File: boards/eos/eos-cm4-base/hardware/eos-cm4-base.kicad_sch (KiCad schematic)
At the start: 43 parts, among them J1 CM4 1-100, J2 CM4 101-200, J3 USB-C, J4 USB-A, J5 TRJG0926HENL, J6 microSD, J7 GPIO, J8 FAN, J9 BOOT, Q1 BSS84, SW1 RESET, U1 USBLC6-2SC6, U2 TPS2041B, U3 USBLC6-2SC6, U4 TPD4EUSB30, U5 TPD4EUSB30, U6 RT9742GGJ5, U7 TS3USB30E

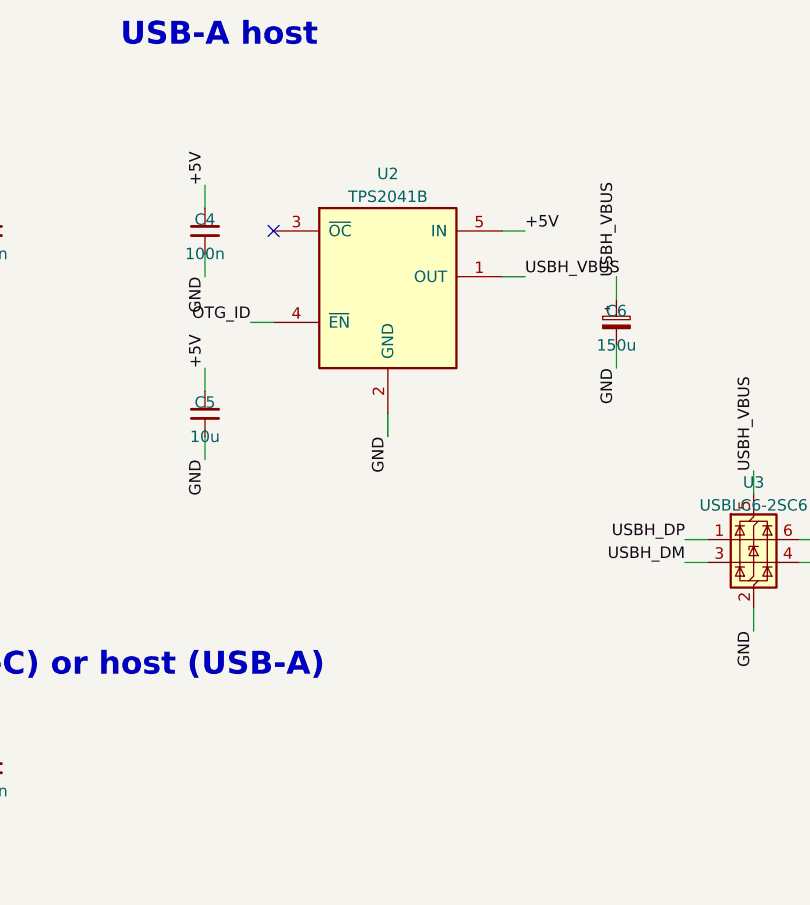
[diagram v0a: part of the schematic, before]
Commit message: feat(boards): EoS Motion Wing and EoS ESP32 DevKit; CM4 USB rework; build fixes
Two more original boards, for catalogue entries whose CAD can't be mirrored. Both were drafted
from chip datasheets and published form-factor specs (no vendor design file), then built and
independently reviewed:
- EoS Motion Wing, a FeatherWing. ADXL343 and ADT7410 on I2C, removable pull-ups,
  address/interrupt jumpers. The outline and headers come from Adafruit's Feather spec. New
  symbol EoS_Sensors:ADT7410 (pins from the ADT7410 datasheet Rev. C, Table 4).
- EoS ESP32 DevKit. ESP32-WROOM-32E with KiCad's own symbol, its stacked GND pin expanded to
  four pads. CP2102N with the esptool auto-program pair, AP7361C. A PMEG6010CEH and a 5.1 kohm
  bleed keep VBUS below the CP2102N's VIL with no host.

EoS CM4 Base, after review:
- The USB-A port moved to the top edge, beside the module's USB pins. The host path fell from
  116/98 mm to 46/35 mm (TI's limit is 101.6 mm).
- USB-A power now comes from a TPS2051C driven through a 2N7002, so it is on only in host mode
  and only with the CM4's 3.3 V up. The old active-low switch turned on when that rail was down.
- 0.1 uF at the switch output, as in TI's application circuit.
- The README now covers the OS's otg_mode and dr_mode, 5 V / 3 A, and the HAT back-feed warning.

Generator fixes, each found on these boards:
- Stacked pin numbers: strict parsing and expansion.
- KiCad's no-connect net names ({slash}, unnamed pins).
- Pre-routes and repairs at the net class width.
- ROUTER_MARGIN 0.01 mm, and necks below the minimum widened (locked copper excepted).
- Clearance clashes between routed items ripped up and repaired.
- Silkscreen stroke at least 0.15 mm.

Tests:
- SpecTest, ClashTest, and FigureFourTest: the carriers' holes and connectors placed from
  Figure 4's dimensions alone.
- Intent tests for the CM4, Motion Wing and ESP32.
- Every board README's results table checked against its build report.

All built boards: ERC 0, DRC errors 0, 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
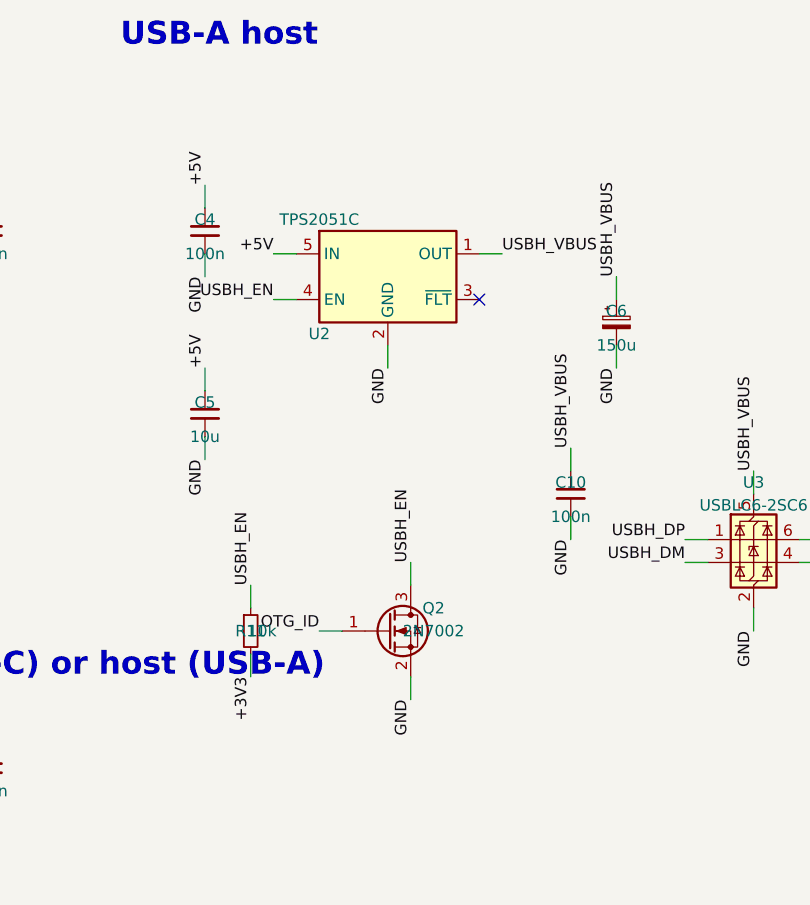
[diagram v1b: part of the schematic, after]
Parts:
- added C10: 100n, Capacitor_SMD:C_0402_1005Metric, symbol Device:C_Small
- added Q2: 2N7002, Package_TO_SOT_SMD:SOT-23, symbol Transistor_FET:2N7002
- added R11: 10k, Resistor_SMD:R_0402_1005Metric, symbol Device:R_Small
- J4: footprint Connector_USB:USB_A_Molex_67643_Horizontal -> Connector_USB:USB_A_Molex_105057_Vertical; MPN 67643-0910 -> 105057-0001
- U2: value TPS2041B -> TPS2051C; symbol Power_Management:TPS2041B -> Power_Management:TPS2051CDBV; MPN TPS2041BDBVR -> TPS2051CDBVR
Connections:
- net +3V3: now also R11.2
- net GND: now also C10.2, Q2.2 (S)
- net OTG_ID: now also Q2.1 (G); no longer U2.4 (~{EN})
- net USBH_VBUS: now also C10.1
- new net USBH_EN: Q2.3 (D), R11.1, U2.4 (EN)
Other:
- moved on the sheet: U2
